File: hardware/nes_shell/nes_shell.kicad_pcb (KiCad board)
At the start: 4 copper layers, 99 x 45 mm, 35 parts, among them J1 USB_C_Receptacle_USB2.0, J2 Micro_SD_Card, Q3 S8050, SW1 SW_Push, SW2 SW_Push, SW3 SW_Push, SW4 SW_Push, SW5 SW_Push, SW6 SW_Push, SW7 SW_Push, SW8 SW_Push, U12 STM32G031G8Ux, U2 STM32H7B0VBTx, U8 REF3033, U9 RT9193-33GB, Y1 Crystal_GND24, Y3 Crystal

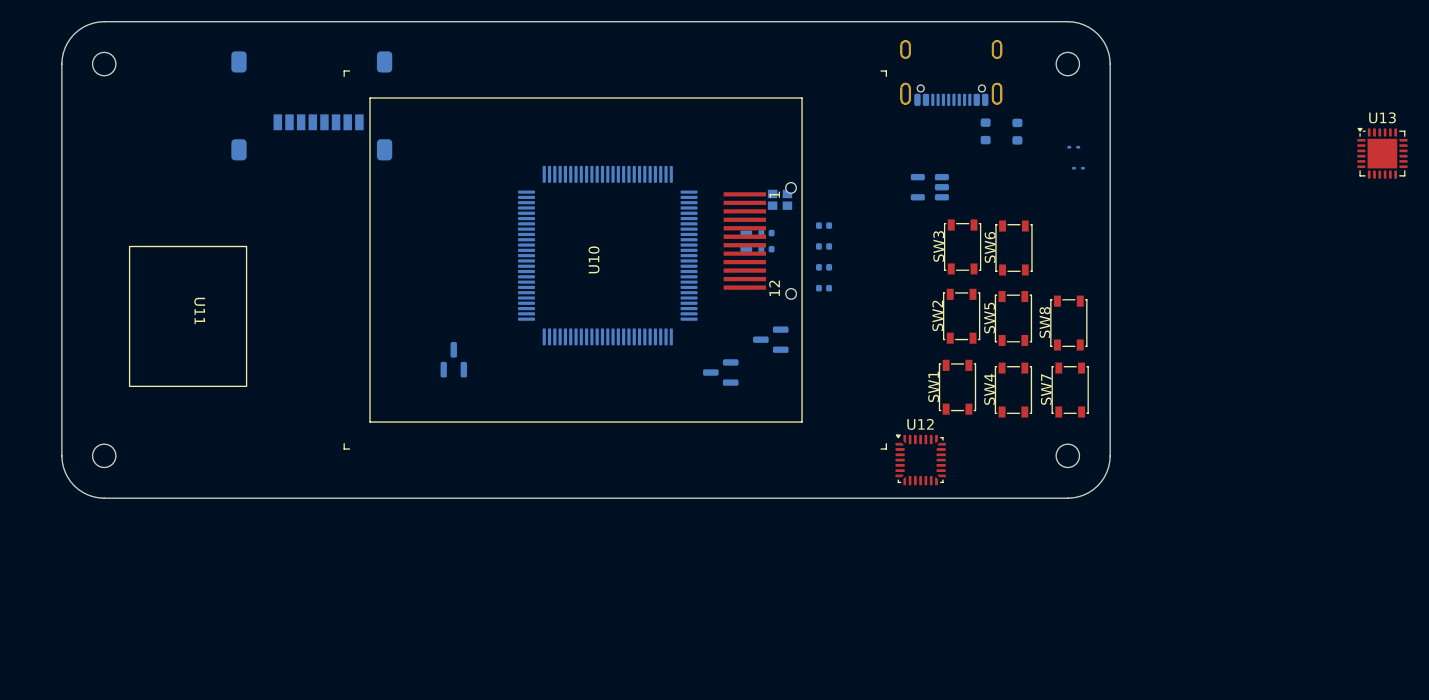
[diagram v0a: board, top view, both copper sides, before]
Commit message: 全新的分离设计，将不同的板子分在不同的项目当中
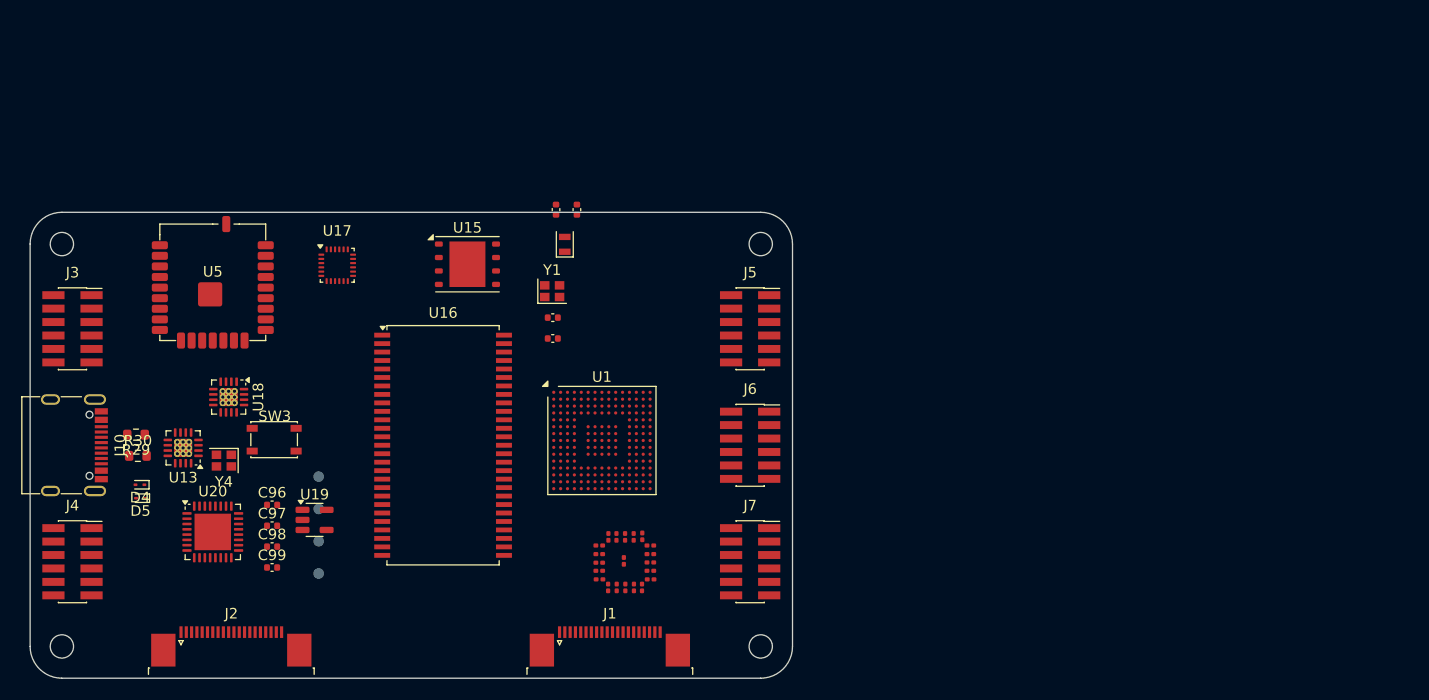
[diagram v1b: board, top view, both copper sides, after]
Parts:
- removed C1, C2: 1.5pF, Capacitor_SMD:C_0402_1005Metric
- removed C3, C4: 8pF, Capacitor_SMD:C_0402_1005Metric
- removed D1: BAT54C, Package_TO_SOT_SMD:SOT-23
- removed D3: ESD9B3.3ST5G, Diode_SMD:D_SOD-923
- removed Q3: S8050, Package_TO_SOT_SMD:SOT-23
- removed R1: 10k, Capacitor_SMD:C_0402_1005Metric
- removed R6, R7: 5.1K, Resistor_SMD:R_0603_1608Metric
- removed SW1, SW2, SW4, SW5, SW6, SW7, SW8: SW_Push, my_footprint:KEY-SMD_4P-L4.2-W3.4-P2.15-LS4.5-TL
- removed U10: ~, my_footprint:ips_2.0_240x320_12p
- removed U11: ~, my_footprint:ns_joystick
- removed U12: STM32G031G8Ux, Package_DFN_QFN:QFN-28_4x4mm_P0.5mm
- removed U2: STM32H7B0VBTx, Package_QFP:LQFP-100_14x14mm_P0.5mm
- removed U8: REF3033, Package_TO_SOT_SMD:SOT-23
- removed U9: RT9193-33GB, Package_TO_SOT_SMD:SOT-23-5
- removed Y3: Crystal, Crystal:Crystal_SMD_2012-2Pin_2.0x1.2mm
- added C10: 0.1uF, Capacitor_SMD:C_0201_0603Metric, F.Cu at (145.6, 111.9)
- added C11: 0.1uF, Capacitor_SMD:C_0201_0603Metric, F.Cu at (145.6, 112.7)
- added C12: 0.1uF, Capacitor_SMD:C_0201_0603Metric, F.Cu at (144.8, 113.4)
- added C13: 0.1uF, Capacitor_SMD:C_0201_0603Metric, F.Cu at (144.0, 113.4)
- added C14: 0.1uF, Capacitor_SMD:C_0201_0603Metric, F.Cu at (142.4, 113.4)
- added C15: 0.1uF, Capacitor_SMD:C_0201_0603Metric, F.Cu at (141.6, 113.4)
- added C16: 0.1uF, Capacitor_SMD:C_0201_0603Metric, F.Cu at (140.8, 112.7)
- added C17: 0.1uF, Capacitor_SMD:C_0201_0603Metric, F.Cu at (140.7, 111.9)
- added C18: 1.5pF, Capacitor_SMD:C_0402_1005Metric, F.Cu at (138.6, 77.8)
- added C19: 0.1uF, Capacitor_SMD:C_0201_0603Metric, F.Cu at (140.7, 111.1)
- added C20: 0.1uF, Capacitor_SMD:C_0201_0603Metric, F.Cu at (140.7, 110.3)
- added C21: 0.1uF, Capacitor_SMD:C_0201_0603Metric, F.Cu at (140.7, 109.5)
- added C22: 0.1uF, Capacitor_SMD:C_0201_0603Metric, F.Cu at (141.6, 108.7)
- added C23: 0.1uF, Capacitor_SMD:C_0201_0603Metric, F.Cu at (142.4, 108.7)
- added C24: 0.1uF, Capacitor_SMD:C_0201_0603Metric, F.Cu at (143.2, 108.7)
- added C25: 0.1uF, Capacitor_SMD:C_0201_0603Metric, F.Cu at (144.0, 108.7)
- added C26: 0.1uF, Capacitor_SMD:C_0201_0603Metric, F.Cu at (144.8, 108.6)
- added C27: 0.1uF, Capacitor_SMD:C_0201_0603Metric, F.Cu at (145.6, 111.1)
- added C28: 0.1uF, Capacitor_SMD:C_0201_0603Metric, F.Cu at (143.2, 113.4)
- added C29: 0.1uF, Capacitor_SMD:C_0201_0603Metric, F.Cu at (143.1, 110.9)
- added C6: 8pF, Capacitor_SMD:C_0402_1005Metric, F.Cu at (136.4, 87.9)
- added C7: 8pF, Capacitor_SMD:C_0402_1005Metric, F.Cu at (136.4, 89.9)
- added C8: 0.1uF, Capacitor_SMD:C_0201_0603Metric, F.Cu at (145.6, 109.5)
- added C9: 0.1uF, Capacitor_SMD:C_0201_0603Metric, F.Cu at (145.6, 110.3)
- added C96: 4.7uF, Capacitor_SMD:C_0402_1005Metric, F.Cu at (109.9, 105.6)
- added C97: 0.1uF, Capacitor_SMD:C_0402_1005Metric, F.Cu at (109.9, 107.6)
- added C98: 22nF, Capacitor_SMD:C_0402_1005Metric, F.Cu at (109.9, 109.6)
- added C99: 4.7uF, Capacitor_SMD:C_0402_1005Metric, F.Cu at (109.9, 111.5)
- added D5: ESD9B3.3ST5G, Diode_SMD:D_SOD-923, F.Cu at (97.4, 105.0)
- added J10: USB_C_Receptacle_USB2.0_16P, Connector_USB:USB_C_Receptacle_G-Switch_GT-USB-7010ASV, F.Cu at (90.0, 100.0)
- added J3: Conn_02x06_Odd_Even, Connector_PinSocket_1.27mm:PinSocket_2x06_P1.27mm_Vertical_SMD, F.Cu at (91.0, 89.0)
- added J4: Conn_02x06_Odd_Even, Connector_PinSocket_1.27mm:PinSocket_2x06_P1.27mm_Vertical_SMD, F.Cu at (91.0, 111.0)
- added J5: Conn_02x06_Odd_Even, Connector_PinSocket_1.27mm:PinSocket_2x06_P1.27mm_Vertical_SMD, F.Cu at (155.0, 89.0)
- added J6: Conn_02x06_Odd_Even, Connector_PinSocket_1.27mm:PinSocket_2x06_P1.27mm_Vertical_SMD, F.Cu at (155.0, 100.0)
- added J7: Conn_02x06_Odd_Even, Connector_PinSocket_1.27mm:PinSocket_2x06_P1.27mm_Vertical_SMD, F.Cu at (155.0, 111.0)
- added R29: 5.1K, Resistor_SMD:R_0603_1608Metric, F.Cu at (97.0, 99.0)
- added R30: 5.1K, Resistor_SMD:R_0603_1608Metric, F.Cu at (97.2, 101.0)
- added TP5: hub_ldo_3v3, TestPoint:TestPoint_Pad_D1.0mm, B.Cu at (114.3, 103.0)
- added TP6: hub_gnd, TestPoint:TestPoint_Pad_D1.0mm, B.Cu at (114.3, 106.0)
- added TP7: DMU, TestPoint:TestPoint_Pad_D1.0mm, B.Cu at (114.3, 109.1)
- added TP8: DPU, TestPoint:TestPoint_Pad_D1.0mm, B.Cu at (114.3, 112.1)
- added U1: STM32H7B0IBKxQ, Package_BGA:UFBGA-201_10x10mm_Layout15x15_P0.65mm, F.Cu at (141.0, 99.5)
- added U15: W25Q32JVZP, Package_SON:WSON-8-1EP_6x5mm_P1.27mm_EP3.4x4.3mm, F.Cu at (128.3, 82.9)
- added U16: MT48LC16M16A2TG, Package_SO:TSOP-II-54_22.2x10.16mm_P0.8mm, F.Cu at (126.0, 100.0)
- added U17: MPU-9250, Sensor_Motion:InvenSense_QFN-24_3x3mm_P0.4mm, F.Cu at (116.0, 83.0)
- added U18: CH343P, Package_DFN_QFN:QFN-16-1EP_3x3mm_P0.5mm_EP1.7x1.7mm_ThermalVias, F.Cu at (105.8, 95.5)
- added U19: RT9193-33GB, Package_TO_SOT_SMD:SOT-23-5, F.Cu at (113.9, 107.0)
- added U20: USB3300-EZK, Package_DFN_QFN:QFN-32-1EP_5x5mm_P0.5mm_EP3.45x3.45mm, F.Cu at (104.2, 108.2)
- added U5: M0S, my_chips:M0S, F.Cu at (104.3, 85.1)
- added Y2: Crystal, Crystal:Crystal_SMD_2012-2Pin_2.0x1.2mm, F.Cu at (137.5, 81.0)
- added Y4: 12M, Crystal:Crystal_SMD_2016-4Pin_2.0x1.6mm, F.Cu at (105.3, 101.5)
- C5: value 100nF -> 1.5pF; moved to F.Cu
- D4, Y1: moved to F.Cu
- J1: value USB_C_Receptacle_USB2.0 -> Conn_01x20_MountingPin; footprint Connector_USB:USB_C_Receptacle_GCT_USB4105-xx-A_16P_TopMnt_Horizontal -> Connector_FFC-FPC:TE_2-1734839-0_1x20-1MP_P0.5mm_Horizontal; moved to F.Cu
- J2: value Micro_SD_Card -> Conn_01x20_MountingPin; footprint Connector_Card:microSD_HC_Molex_47219-2001 -> Connector_FFC-FPC:TE_2-1734839-0_1x20-1MP_P0.5mm_Horizontal; moved to F.Cu
- U13: value ~ -> CH334P; footprint Package_DFN_QFN:QFN-24-1EP_4x4mm_P0.5mm_EP2.8x2.8mm -> Package_DFN_QFN:QFN-16-1EP_3x3mm_P0.5mm_EP1.7x1.7mm_ThermalVias
- moved U13 116.6 mm to (101.5, 100.2), turned to 180 degrees
- moved D4 93.5 mm to (97.4, 103.7)
- moved SW3 67.6 mm to (110.1, 99.5), turned to 0 degrees
- moved J1 64.0 mm to (141.8, 119.0)
- moved J2 52.2 mm to (106.0, 119.0)
- moved H4 34.1 mm to (156.0, 119.0)
- moved H2 33.6 mm to (156.0, 81.0)
- moved C5 25.9 mm to (136.7, 77.8), turned to 90 degrees
- moved Y1 23.2 mm to (136.3, 85.5), turned to 0 degrees
- moved H3 18.4 mm to (90.0, 119.0)
- moved H1 17.5 mm to (90.0, 81.0)
- renumbered H3 to H2, H2 to H3
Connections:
- C5 pad 1: /NRST -> /OSC32_IN
- D4 pad 2: /usb1_D- -> /USB通信/USB_D-
- J2 pad 1: /SD1_D2 -> unconnected-(J2-Pin_1-Pad1)
- J2 pad 2: /SD1_D3 -> unconnected-(J2-Pin_2-Pad2)
- J2 pad 3: /SD1_CMD -> unconnected-(J2-Pin_3-Pad3)
- J2 pad 5: /SD1_CLK -> unconnected-(J2-Pin_5-Pad5)
- J2 pad 7: /SD1_D0 -> unconnected-(J2-Pin_7-Pad7)
- J2 pad 8: /SD1_D1 -> unconnected-(J2-Pin_8-Pad8)
- SW3 pad 1: unconnected-(SW3-Pad1) -> /USB通信/M0S-daplink/BOOT
- SW3 pad 2: unconnected-(SW3-Pad2) -> +3V3
- U13 pad 1: unconnected-(U13-ANT-Pad1) -> Net-(U13-XO)
- U13 pad 10: unconnected-(U13-MTDI-Pad10) -> /USB通信/M0S-daplink/USB_DP
- U13 pad 11: unconnected-(U13-VDD3P3_RTC-Pad11) -> /USB通信/USB_D-
- U13 pad 12: unconnected-(U13-MTCK-Pad12) -> /USB通信/USB_D+
- U13 pad 15: unconnected-(U13-GPIO9-Pad15) -> /USB通信/RT9193/+3V3
- U13 pad 16: unconnected-(U13-GPIO10-Pad16) -> /USB通信/RT9193/+3V3
- U13 pad 17: unconnected-(U13-VDD3P3_CPU-Pad17) -> (no net)
- U13 pad 2: unconnected-(U13-VDDA3P3-Pad2) -> Net-(U13-XI)
- U13 pad 7: unconnected-(U13-CHIP_EN-Pad7) -> /USB通信/CH343P/D-
- U13 pad 8: unconnected-(U13-GPIO3-Pad8) -> /USB通信/CH343P/D+
- U13 pad 9: unconnected-(U13-MTMS-Pad9) -> /USB通信/M0S-daplink/USB_DM
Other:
- board size 99 x 45 mm -> 72 x 44 mm
- copper layers 4 -> 6
